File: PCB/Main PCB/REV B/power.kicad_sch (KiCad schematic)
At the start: 14 parts, among them Q3 Q_PMOS_GSD, Q4 Q_PMOS_GSD, U8 AMS1117-3.3, U9 LTC4412xS6

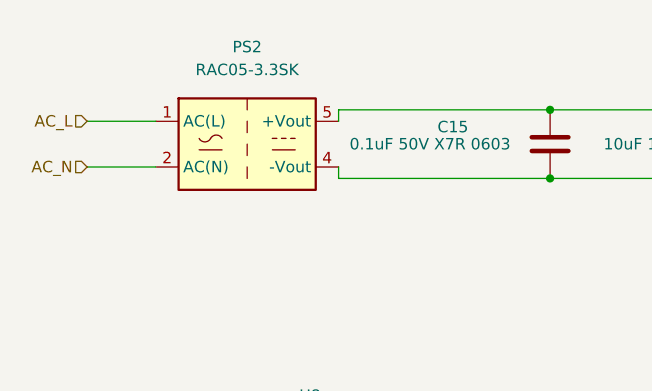
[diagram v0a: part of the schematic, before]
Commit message: Component changes, new relays
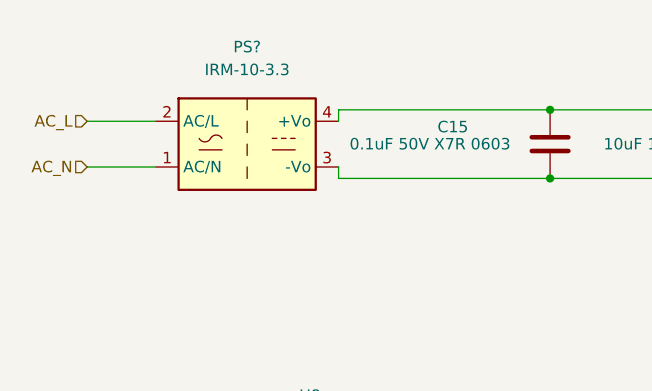
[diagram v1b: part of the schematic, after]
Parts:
- removed PS2: RAC05-3.3SK, Converter_ACDC:Converter_ACDC_RECOM_RAC05-xxSK_THT, symbol Converter_ACDC:RAC05-3.3SK
- added PS?: IRM-10-3.3, Converter_ACDC:Converter_ACDC_MeanWell_IRM-10-xx_THT, symbol Converter_ACDC:IRM-10-3.3
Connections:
- net +3.3VA: now also PS?.4 (+Vo)
- net AC_L: now also PS?.2 (AC/L)
- net AC_N: now also PS?.1 (AC/N)
- net GND: now also PS?.3 (-Vo)
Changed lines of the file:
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@@
     (pin "1")
-  )
-  (symbol (lib_id "Converter_ACDC:RAC05-3.3SK") (at 49.53 43.18 0) (unit 1)
-    (in_bom yes) (on_board yes) (fields_autoplaced)
-    (property "Reference" "PS2" (id 0) (at 49.53 32.385 0))
-    (property "Value" "RAC05-3.3SK" (id 1) (at 49.53 34.925 0))
-    (property "Footprint" "Converter_ACDC:Converter_ACDC_RECOM_RAC05-xxSK_THT" (id 2) (at 49.53 52.07 0)
-      (effects (font (size 1.27 1.27)) hide)
-    )
-    (property "Datasheet" "https://www.recom-power.com/pdf/Powerline-AC-DC/RAC05-K.pdf" (id 3) (at 46.99 35.56 0)
-      (effects (font (size 1.27 1.27)) hide)
-    )
-    (property "Manufacturer" "Recom Power" (id 4) (at 49.53 43.18 0)
-      (effects (font (size 1.27 1.27)) hide)
-    )
-    (property "Manufacturer Part Number" "RAC05-3.3SK" (id 5) (at 49.53 43.18 0)
-      (effects (font (size 1.27 1.27)) hide)
-    )
-    (property "Vendor" "Digikey" (id 6) (at 49.53 43.18 0)
-      (effects (font (size 1.27 1.27)) hide)
-    )
-    (property "Vendor Part Number" "945-3116-5-ND" (id 7) (at 49.53 43.18 0)
-      (effects (font (size 1.27 1.27)) hide)
-    )
-    (pin "1")
-    (pin "2")
-    (pin "3")
-    (pin "4")
-    (pin "5")
   )
   (symbol (lib_id "Device:C") (at 67.945 83.82 0) (mirror y) (unit 1)
@@
     (pin "2")
   )
+  (symbol (lib_id "Converter_ACDC:IRM-10-3.3") (at 49.53 43.18 0) (unit 1)
+    (in_bom yes) (on_board yes) (fields_autoplaced)
+    (property "Reference" "PS?" (id 0) (at 49.53 32.385 0))
+    (property "Value" "IRM-10-3.3" (id 1) (at 49.53 34.925 0))
+    (property "Footprint" "Converter_ACDC:Converter_ACDC_MeanWell_IRM-10-xx_THT" (id 2) (at 49.53 52.07 0)
+      (effects (font (size 1.27 1.27)) hide)
+    )
+    (property "Datasheet" "https://www.meanwell.com/Upload/PDF/IRM-10/IRM-10-SPEC.PDF" (id 3) (at 49.53 53.34 0)
+      (effects (font (size 1.27 1.27)) hide)
+    )
+    (property "Manufacturer" "MEAN WELL USA Inc." (id 4) (at 49.53 43.18 0)
+      (effects (font (size 1.27 1.27)) hide)
+    )
+    (property "Manufacturer Part Number" "IRM-10-3.3" (id 5) (at 49.53 43.18 0)
+      (effects (font (size 1.27 1.27)) hide)
+    )
+    (property "Vendor" "Digikey" (id 6) (at 49.53 43.18 0)
+      (effects (font (size 1.27 1.27)) hide)
+    )
+    (property "Vendor Part Number" "1866-3031-ND" (id 7) (at 49.53 43.18 0)
+      (effects (font (size 1.27 1.27)) hide)
+    )
+    (pin "1")
+    (pin "2")
+    (pin "3")
+    (pin "4")
+  )
   (symbol (lib_id "Device:C") (at 83.185 43.18 0) (mirror x) (unit 1)

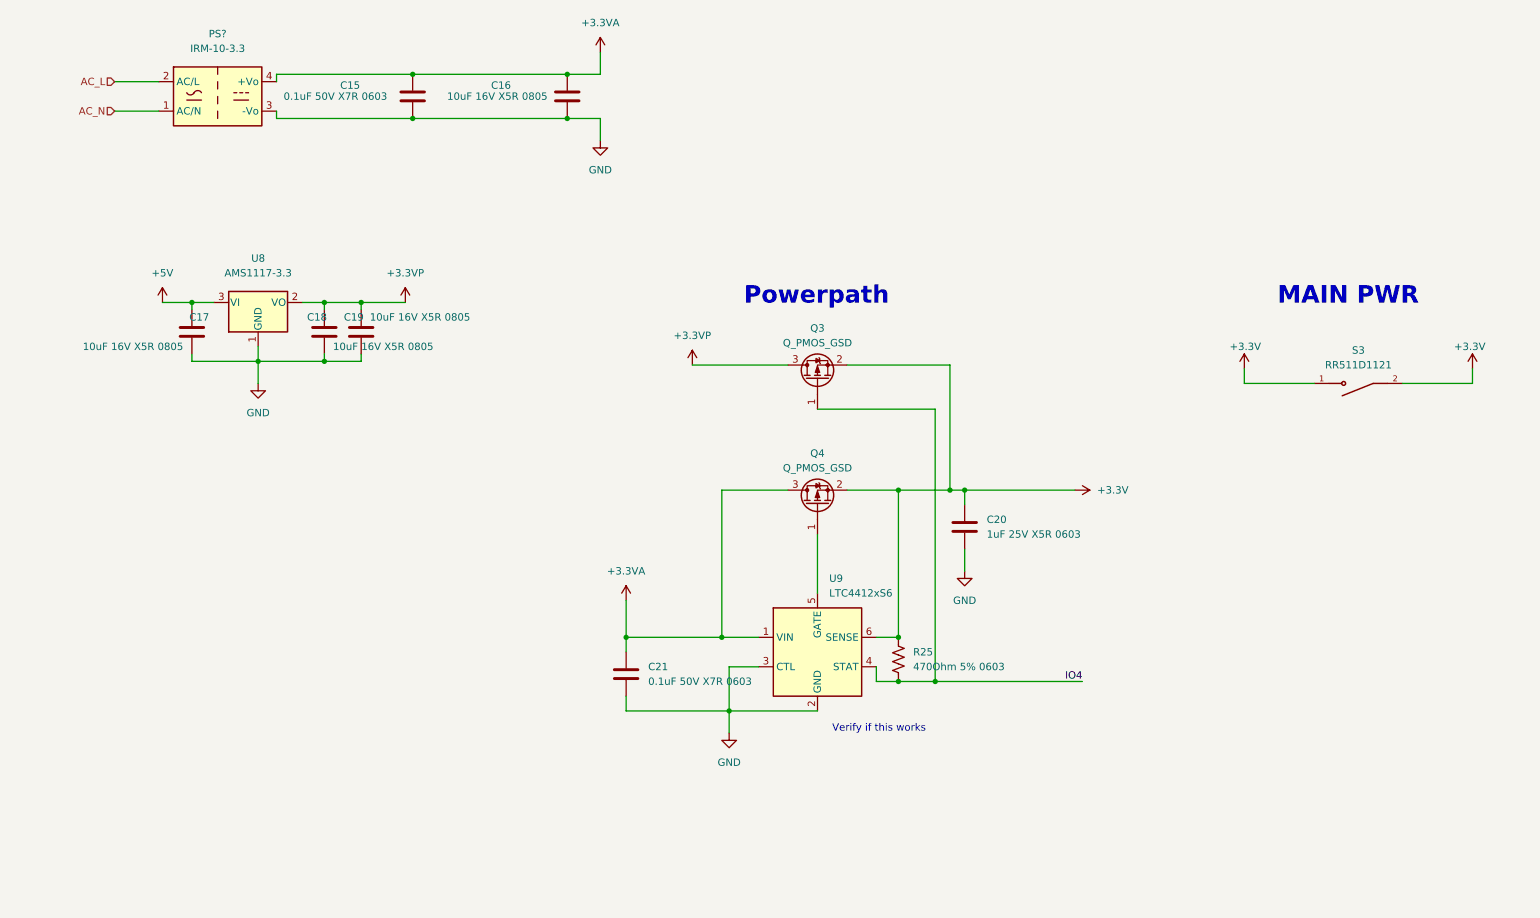
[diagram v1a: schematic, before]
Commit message: Rid power path selector, moving to or diode system for power path selection
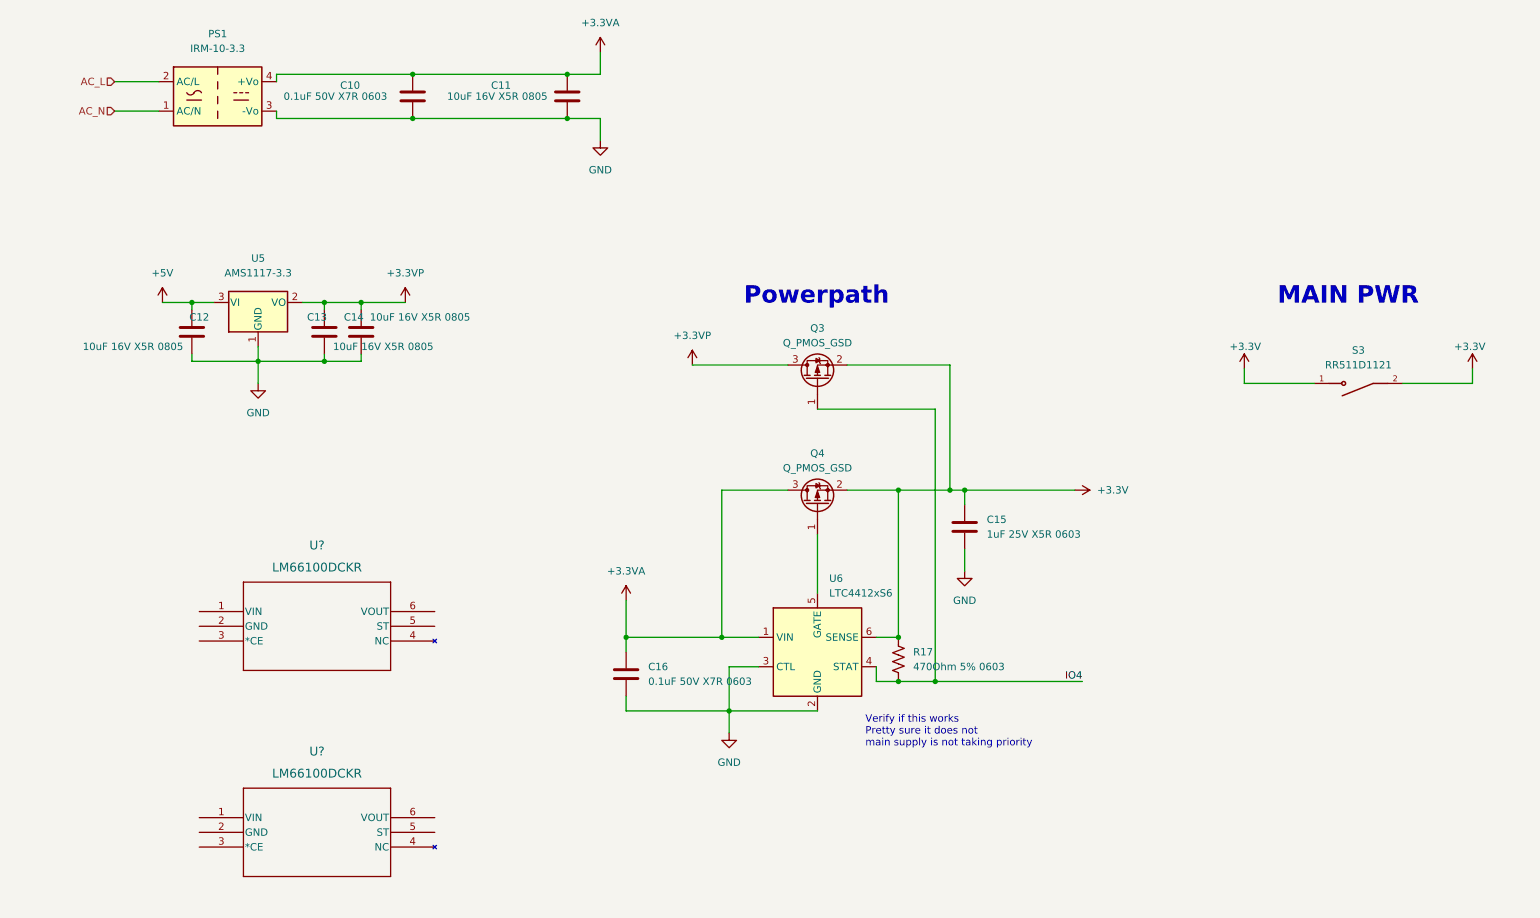
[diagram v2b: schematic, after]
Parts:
- added U? (x2): LM66100DCKR, Customs Smoker:DCK6_TEX, symbol LM66100DCKR:LM66100DCKR
- gave numbers to parts that had none: 1
- renumbered C15 to C10, C16 to C11, C17 to C12, C18 to C13, C19 to C14, C20 to C15, C21 to C16, R25 to R17, U8 to U5, U9 to U6
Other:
- note added: "Verify if this works Pretty sure it does not main supply is not taking priority"
- note removed: "Verify if this works"

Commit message: Powerpath development
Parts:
- removed C15: 1uF 25V X5R 0603, Capacitor_SMD:C_0603_1608Metric, symbol Device:C
- removed C16: 0.1uF 50V X7R 0603, Capacitor_SMD:C_0603_1608Metric, symbol Device:C
- removed Q3, Q4: Q_PMOS_GSD, Package_TO_SOT_SMD:SOT-23, symbol Device:Q_PMOS_GSD
- removed R17: 470Ohm 5% 0603, Resistor_SMD:R_0603_1608Metric, symbol Device:R_US
- removed U6: LTC4412xS6, Package_TO_SOT_SMD:TSOT-23-6, symbol Power_Management:LTC4412xS6
- added C? (x2): 0.1uF 50V X7R 0603, Capacitor_SMD:C_0603_1608Metric, symbol Device:C
- added C?: 1uF 25V X5R 0603, Capacitor_SMD:C_0603_1608Metric, symbol Device:C
- added R?: 470Ohm 5% 0603, Resistor_SMD:R_0603_1608Metric, symbol Device:R_US
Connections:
- net +3.3V: now also U?.6 (VOUT), U?.6 (VOUT), C?.2
- net +3.3VA: now also U?.1 (VIN), U?.3 (*CE), C?.1
- net +3.3VP: now also U?.1 (VIN), C?.1, R?.2
- net GND: now also U?.2 (GND), U?.2 (GND), C?.1, C?.2, C?.2
- net IO4: now also U?.5 (ST)
- net at U?.5 (ST): now also U?.3 (*CE), R?.1
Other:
- note added: "Check Resistors and Capacitors"
- note removed: "Verify if this works Pretty sure it does not main supply is not taking priority"
- moved on the sheet: U?

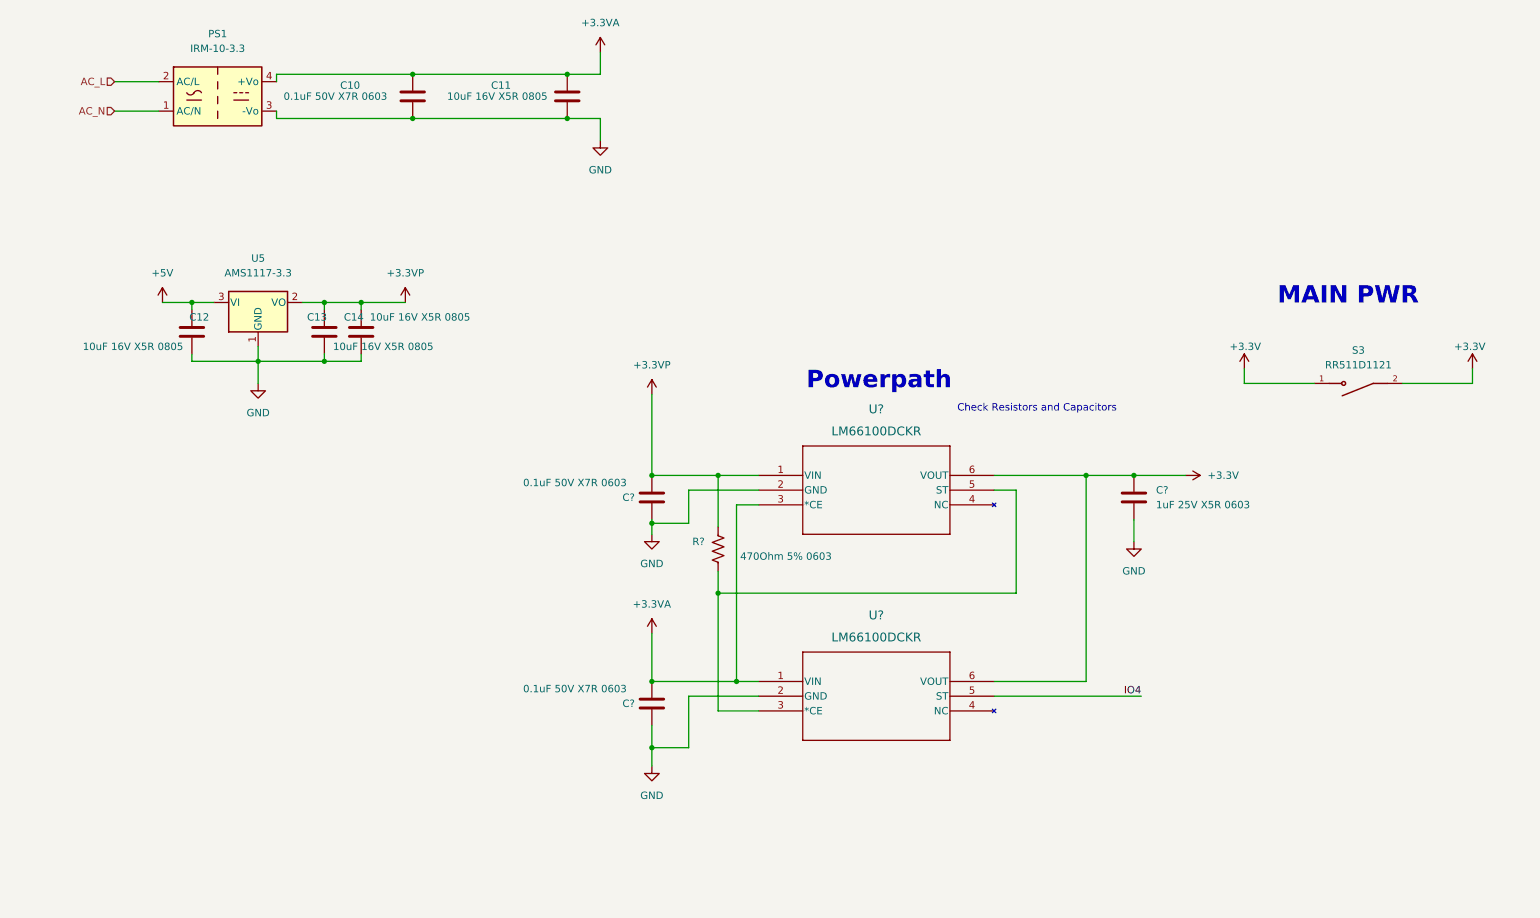
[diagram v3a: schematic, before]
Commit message: Moved from ORing diodes to power MUX as per TI recommendations
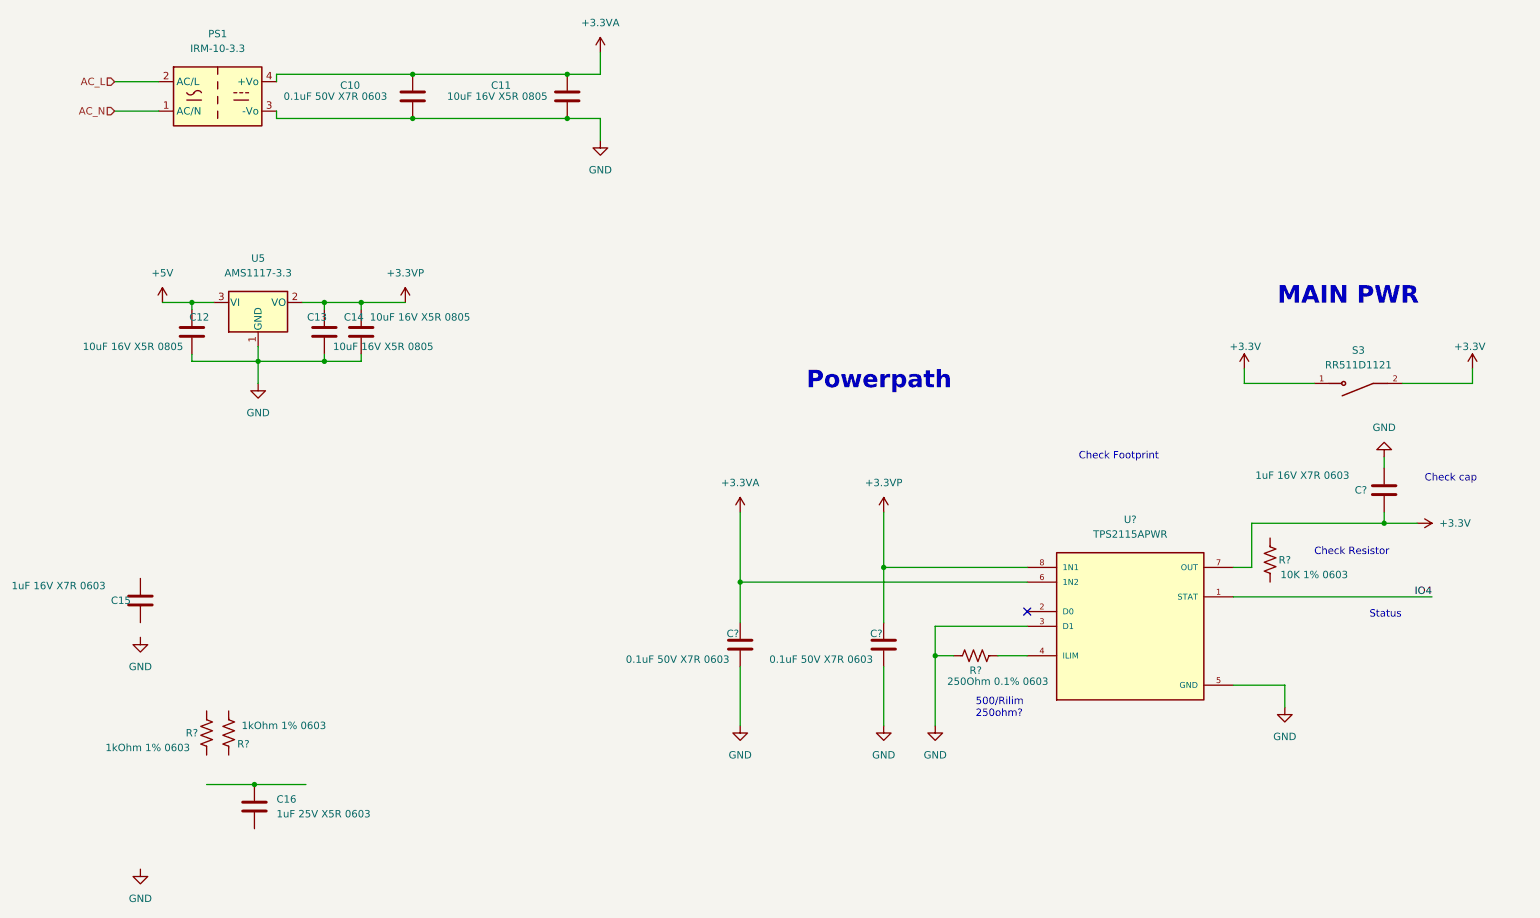
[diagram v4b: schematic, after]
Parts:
- removed C?: 0.1uF 50V X7R 0603, Capacitor_SMD:C_0603_1608Metric, symbol Device:C
- removed R?: 470Ohm 5% 0603, Resistor_SMD:R_0603_1608Metric, symbol Device:R_US
- removed U? (x2): LM66100DCKR, Customs Smoker:DCK6_TEX, symbol LM66100DCKR:LM66100DCKR
- added C? (x2): 0.1uF 50V X7R 0603, Capacitor_SMD:C_0603_1608Metric, symbol Device:C
- added C?: 1uF 16V X7R 0603, Capacitor_SMD:C_0603_1608Metric, symbol Device:C
- added R? (x2): 1kOhm 1% 0603, Resistor_SMD:R_0603_1608Metric, symbol Device:R_US
- added R?: 250Ohm 0.1% 0603, Resistor_SMD:R_0603_1608Metric, symbol Device:R_US
- added R?: 10K 1% 0603, Resistor_SMD:R_0603_1608Metric, symbol Device:R_US
- added U?: TPS2115APWR, Customs Smoker:SOP65P640X120-8N, symbol TPS2115APWR:TPS2115APWR
- C15: renamed from C?; value 0.1uF 50V X7R 0603 -> 1uF 16V X7R 0603; Manufacturer Samsung Electro-Mechanics -> Yageo; Manufacturer Part Number CL10B104KB8NNWC -> CC0603KRX7R7BB105; Vendor Part Number 1276-1935-1-ND -> 311-1446-1-ND
- gave numbers to parts that had none: 1
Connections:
- net +3.3V: now also C?.2, U?.7 (OUT); no longer C16.2
- net +3.3VA: now also C?.2, U?.6 (1N2)
- net +3.3VP: now also C?.2, U?.8 (1N1); no longer C15.1
- net GND: now also C?.1, C?.1, C?.1, R?.2, U?.3 (D1), U?.5 (GND); no longer C15.2, C16.1
- net IO4: now also U?.1 (STAT)
- new net: R?.1, U?.4 (ILIM)
- no-connect marks 0 -> 1
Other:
- note added: "500/Rilim 250ohm?"
- note added: "Check Footprint"
- note added: "Check Resistor"
- note added: "Check cap"
- note added: "Status"
- note removed: "Check Resistors and Capacitors"
- moved on the sheet: C15, C16

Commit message: Power Mux and rest of power systems designed and ready for layout
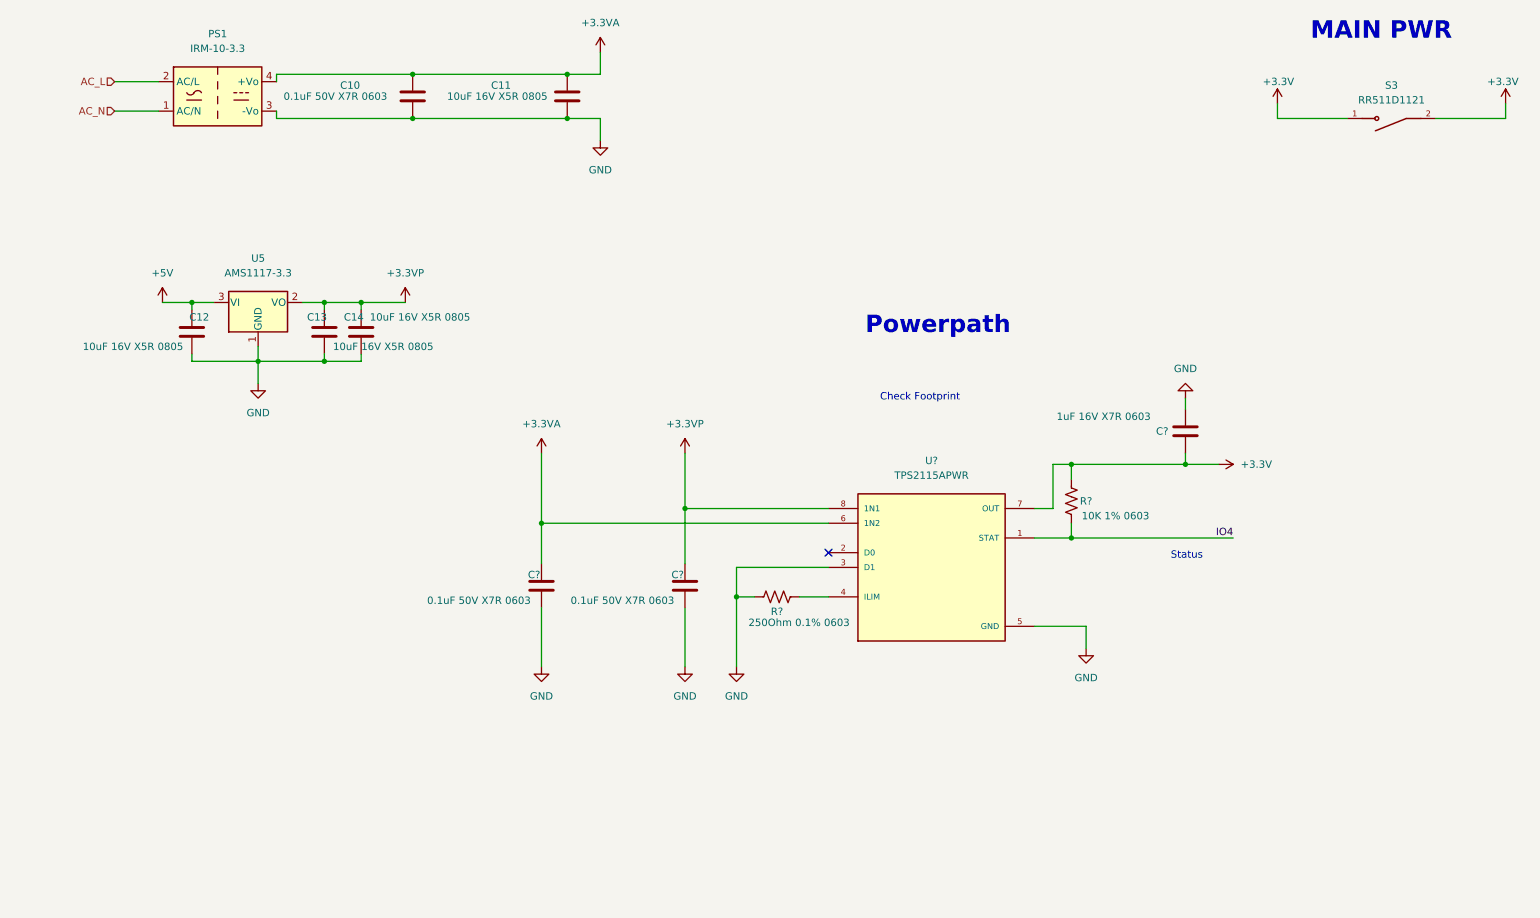
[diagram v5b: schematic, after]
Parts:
- removed C15: 1uF 16V X7R 0603, Capacitor_SMD:C_0603_1608Metric, symbol Device:C
- removed C16: 1uF 25V X5R 0603, Capacitor_SMD:C_0603_1608Metric, symbol Device:C
- removed R? (x2): 1kOhm 1% 0603, Resistor_SMD:R_0603_1608Metric, symbol Device:R_US
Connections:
- net +3.3V: now also R?.1
- net IO4: now also R?.2
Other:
- note removed: "500/Rilim 250ohm?"
- note removed: "Check Resistor"
- note removed: "Check cap"
- moved on the sheet: C?, R?, S3, U?
